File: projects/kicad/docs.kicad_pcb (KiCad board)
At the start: 2 copper layers, 90 x 100 mm, 19 parts, among them SW1 SW_PUSH, SW2 SW_PUSH, SW3 SW_PUSH, SW4 SW_PUSH, SW5 SW_PUSH, SW6 SW_PUSH, SW7 RotaryEncoder_Switch, U1 Pico, U3 2.8_240x320_touch_sd_spi

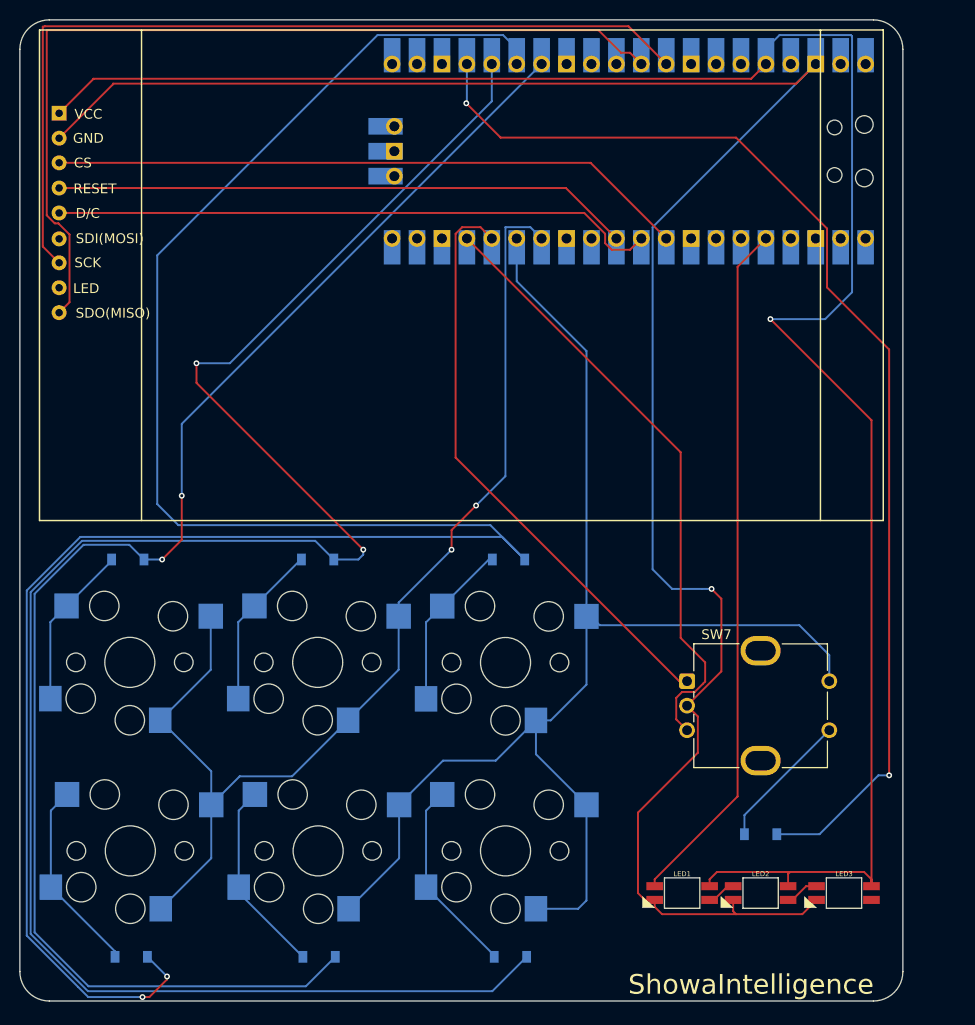
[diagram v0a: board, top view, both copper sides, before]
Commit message: chocolate: 配線を削除
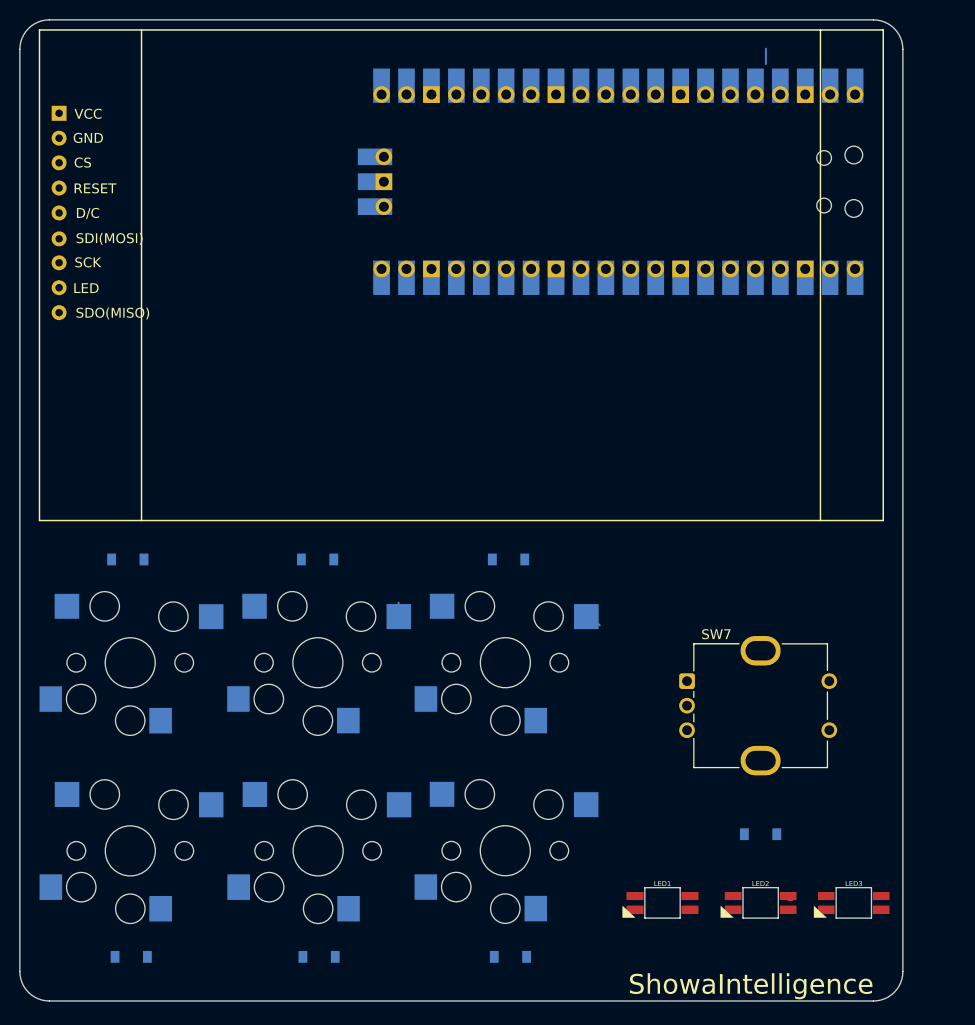
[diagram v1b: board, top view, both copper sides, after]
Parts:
- moved U1 3.29 mm to (149.0, 39.5)
- moved LED1 2.24 mm to (153.5, 113.0)
- moved LED3 1.41 mm to (173.0, 113.0)
- moved LED2 1.00 mm to (163.5, 113.0)
- moved SW1 0.06 mm to (99.2, 88.5)
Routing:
- net Row1: track 223.1 -> 0.00 mm, vias 2 -> 0
- net GND: track 203.0 -> 0.00 mm, vias 1 -> 0
- net 3V3 Out: track 202.8 -> 2.00 mm, vias 1 -> 0
- net Row2: track 197.8 -> 0.00 mm, vias 2 -> 0
- net Row0: track 150.9 -> 0.00 mm, vias 2 -> 0
- net Cal1: track 140.4 -> 1.72 mm
- net Row3: track 118.4 -> 0.00 mm, vias 2 -> 0
- net Cal0: track 114.8 -> 1.39 mm, vias 2 -> 0
- net SDA: track 92.4 -> 0.00 mm
- net SCL: track 89.9 -> 0.00 mm
- net LED: track 71.4 -> 0.00 mm
- net CS: track 65.1 -> 0.00 mm
- net RE_B: track 62.6 -> 0.00 mm
- net DC: track 61.9 -> 0.00 mm
- net RE_A: track 60.3 -> 0.00 mm
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
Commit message: chocolate: 配線図を整理
配線整理に合わせて回路図も一部修正
PCBのデザインルールチェッカーで確認済み：エラー12件
(LEDに関するものでフットプリント時からあり？)
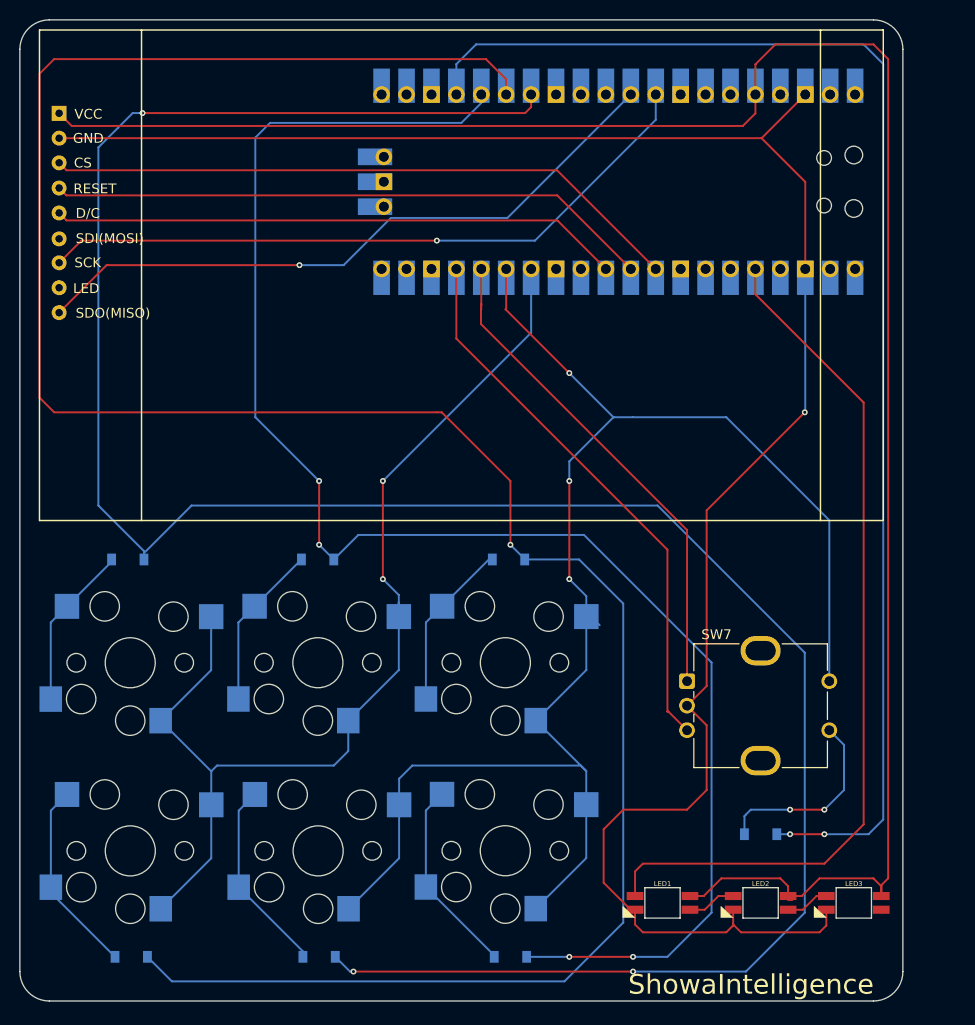
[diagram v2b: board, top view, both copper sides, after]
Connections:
- U1 pad 10: DC -> RST
- U1 pad 11: RST -> DC
- U1 pad 3: unconnected-(U1-GND-Pad3) -> GND
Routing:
- net Row0: track 0.00 -> 244.7 mm, vias 0 -> 3
- net Row1: track 0.00 -> 240.1 mm, vias 0 -> 1
- net 3V3 Out: track 2.00 -> 201.7 mm
- net GND: track 0.00 -> 199.4 mm, vias 0 -> 1
- net Row2: track 0.00 -> 162.8 mm, vias 0 -> 4
- net Cal1: track 1.72 -> 158.5 mm, vias 0 -> 3
- net Row3: track 0.00 -> 136.7 mm, vias 0 -> 2
- net Cal0: track 1.39 -> 110.6 mm, vias 0 -> 2
- net LED: track 0.00 -> 89.0 mm
- net SCL: track 0.00 -> 69.4 mm, vias 0 -> 1
- net SDA: track 0.00 -> 67.5 mm, vias 0 -> 1
- net CS: track 0.00 -> 65.3 mm
- net RST: track 0.00 -> 61.7 mm
- net DC: track 0.00 -> 58.1 mm
- net RE_B: track 0.00 -> 56.8 mm
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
